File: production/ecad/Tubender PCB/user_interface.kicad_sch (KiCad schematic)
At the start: 10 parts, among them IC1 SN74HC138PWR, IC2 RA8875L3N, J7 4-1734592-0, U5 74HC595, U6 PEC11R-4215K-S0024

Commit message: Temp page added
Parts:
- added IC3: SN74LVC1G29DCTR, SOP65P400X130-8N, symbol SamacSys_Parts:SN74LVC1G29DCTR
- added IC4: SN74HC138PWR, SOP65P640X120-16N, symbol SamacSys_Parts:SN74HC138PWR
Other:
- moved on the sheet: DS1, IC1, U5

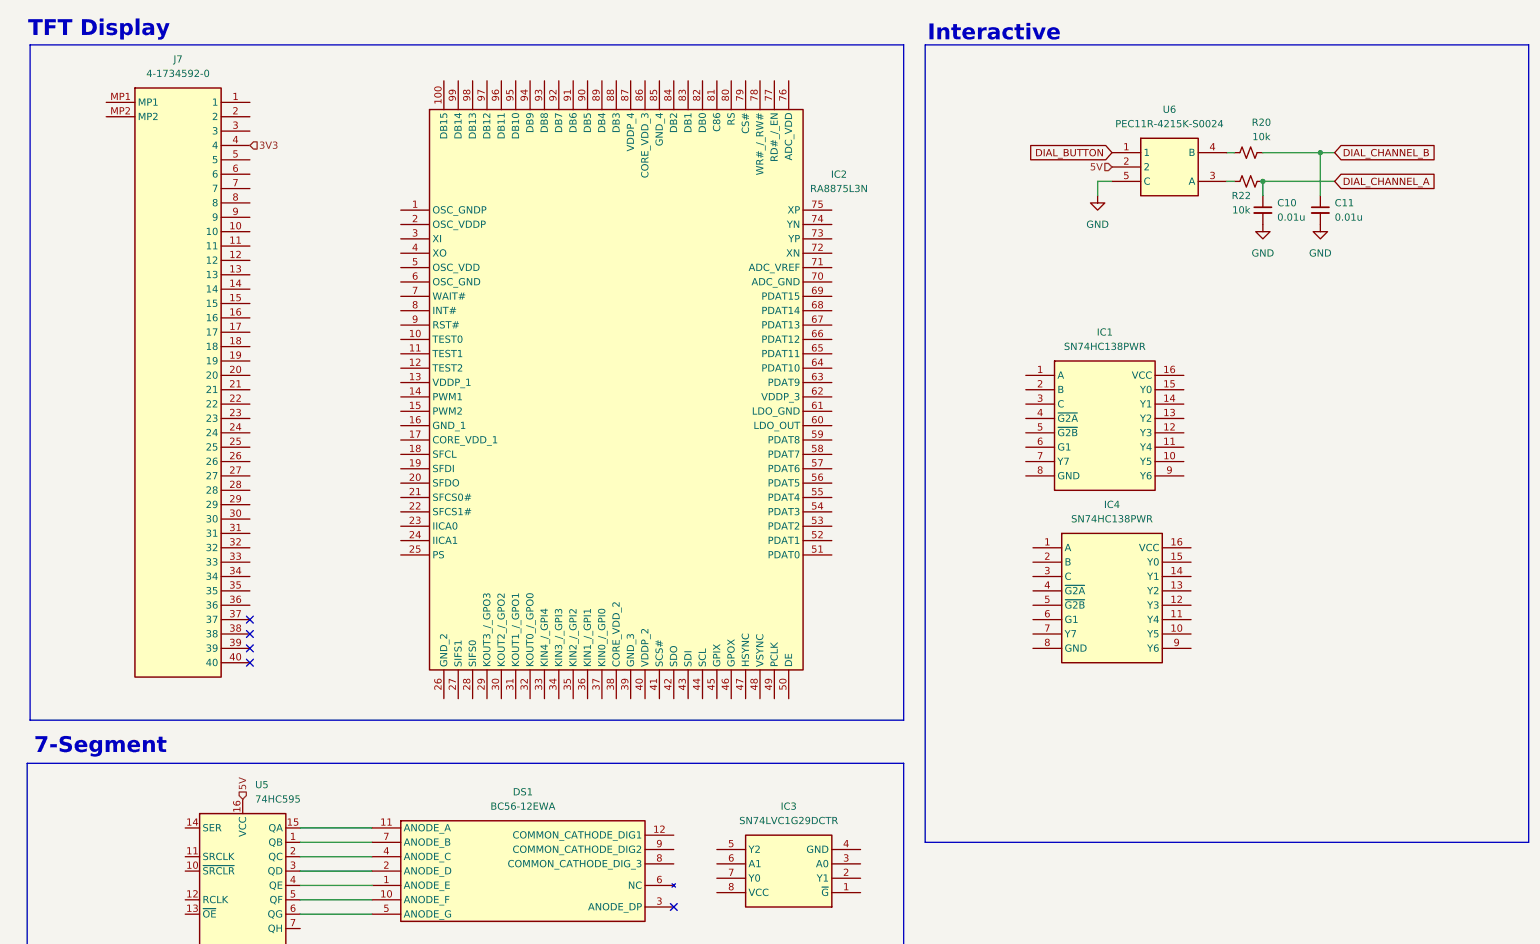
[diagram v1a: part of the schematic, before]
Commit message: Driver pin out
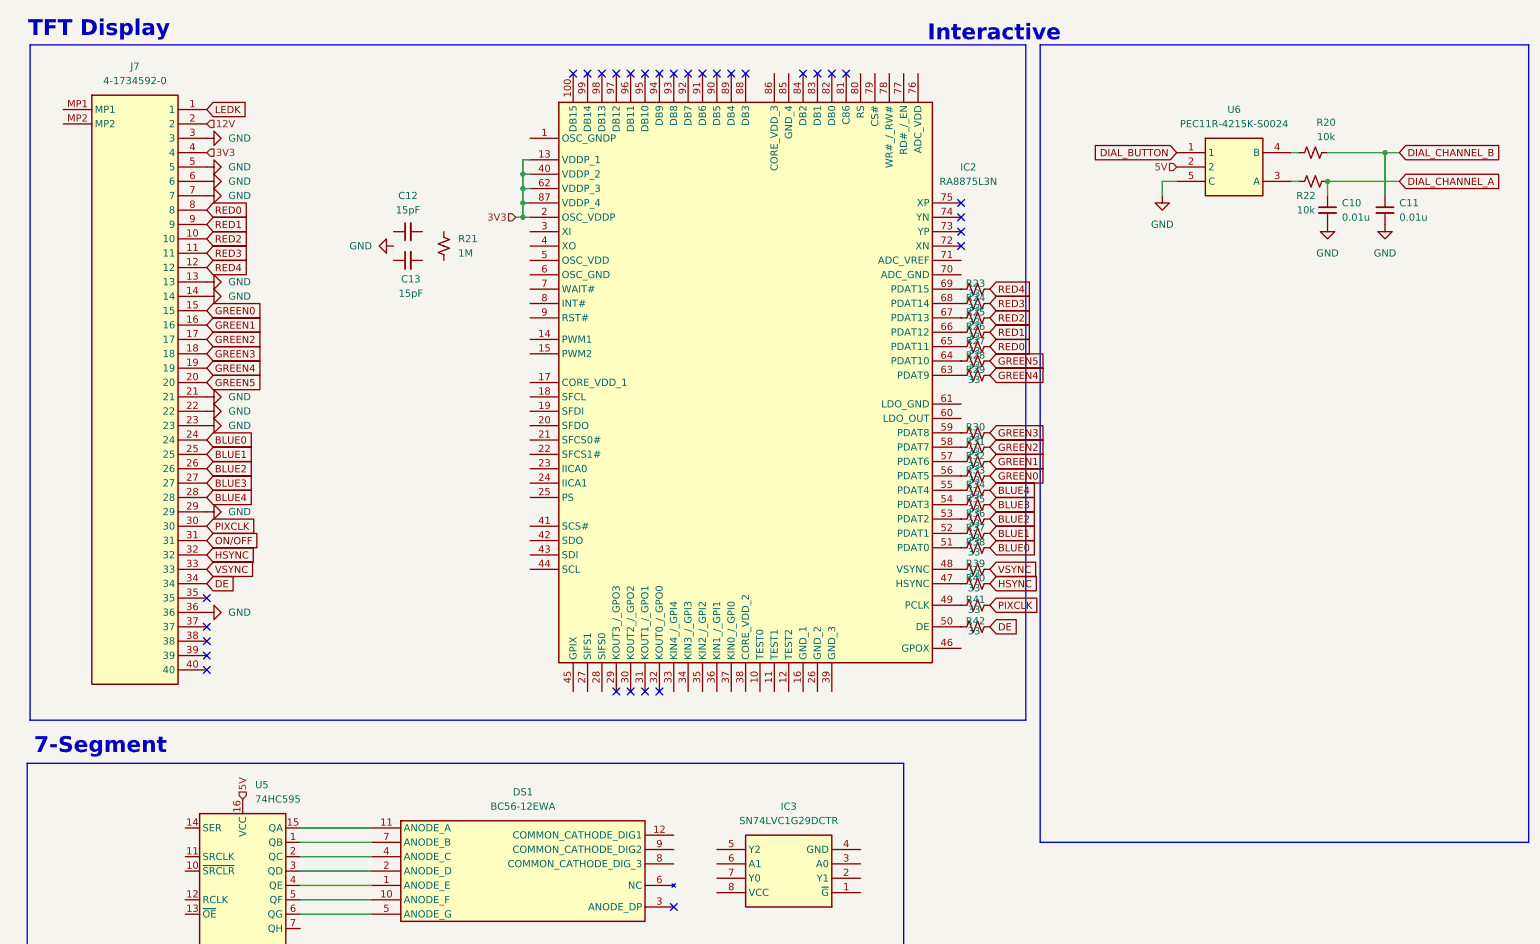
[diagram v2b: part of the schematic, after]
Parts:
- removed IC1, IC4: SN74HC138PWR, SOP65P640X120-16N, symbol SamacSys_Parts:SN74HC138PWR
- added C12, C13: 15pF, symbol Device:C_Small
- added R21: 1M, symbol Device:R_Small_US
- added R23, R24, R25, R26, R27, R28, R29, R30, R31, R32, R33, R34, R35, R36, R37, R38, R39, R40, R41, R42: 33, symbol Device:R_Small_US
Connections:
- net 3V3: now also IC2.13 (VDDP_1), IC2.2 (OSC_VDDP), IC2.40 (VDDP_2), IC2.62 (VDDP_3), IC2.87 (VDDP_4)
- net GND: now also J7.13, J7.14, J7.21, J7.22, J7.23, J7.29, J7.3, J7.36, J7.5, J7.6, J7.7
- net at IC2.47 (HSYNC): now also R40.1
- net at IC2.48 (VSYNC): now also R39.1
- net at IC2.49 (PCLK): now also R41.1
- net at IC2.50 (DE): now also R42.1
- net at IC2.51 (PDAT0): now also R38.1
- net at IC2.52 (PDAT1): now also R37.1
- net at IC2.53 (PDAT2): now also R36.1
- net at IC2.54 (PDAT3): now also R35.1
- net at IC2.55 (PDAT4): now also R34.1
- net at IC2.56 (PDAT5): now also R33.1
- net at IC2.57 (PDAT6): now also R32.1
- net at IC2.58 (PDAT7): now also R31.1
- net at IC2.59 (PDAT8): now also R30.1
- net at IC2.63 (PDAT9): now also R29.1
- net at IC2.64 (PDAT10): now also R28.1
- net at IC2.65 (PDAT11): now also R27.1
- net at IC2.66 (PDAT12): now also R26.1
- net at IC2.67 (PDAT13): now also R25.1
- net at IC2.68 (PDAT14): now also R24.1
- net at IC2.69 (PDAT15): now also R23.1
- net LEDK: now reaches J7.1
- net RED2: now reaches J7.10
- net RED2: now also R25.2
- net RED3: now reaches J7.11
- net RED3: now also R24.2
- net RED4: now reaches J7.12
- net RED4: now also R23.2
- net GREEN0: now reaches J7.15
- net GREEN0: now also R33.2
- net GREEN1: now reaches J7.16
- net GREEN1: now also R32.2
- net GREEN2: now reaches J7.17
- net GREEN2: now also R31.2
- net GREEN3: now reaches J7.18
- net GREEN3: now also R30.2
- net GREEN4: now reaches J7.19
- net GREEN4: now also R29.2
- net 12V: now reaches J7.2
- net GREEN5: now reaches J7.20
- net GREEN5: now also R28.2
- net BLUE0: now reaches J7.24
- net BLUE0: now also R38.2
- net BLUE1: now reaches J7.25
- net BLUE1: now also R37.2
- net BLUE2: now reaches J7.26
- net BLUE2: now also R36.2
- net BLUE3: now reaches J7.27
- net BLUE3: now also R35.2
- net BLUE4: now reaches J7.28
- net BLUE4: now also R34.2
- net PIXCLK: now reaches J7.30
- net PIXCLK: now also R41.2
- net ON/OFF: now reaches J7.31
- net HSYNC: now reaches J7.32
- net HSYNC: now also R40.2
- net VSYNC: now reaches J7.33
- net VSYNC: now also R39.2
- net DE: now reaches J7.34
- net DE: now also R42.2
- net RED0: now reaches J7.8
- net RED0: now also R27.2
- net RED1: now reaches J7.9
- net RED1: now also R26.2
- no-connect marks 5 -> 31
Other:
- moved on the sheet: C10, C11, IC2, J7, R20, R22, U6

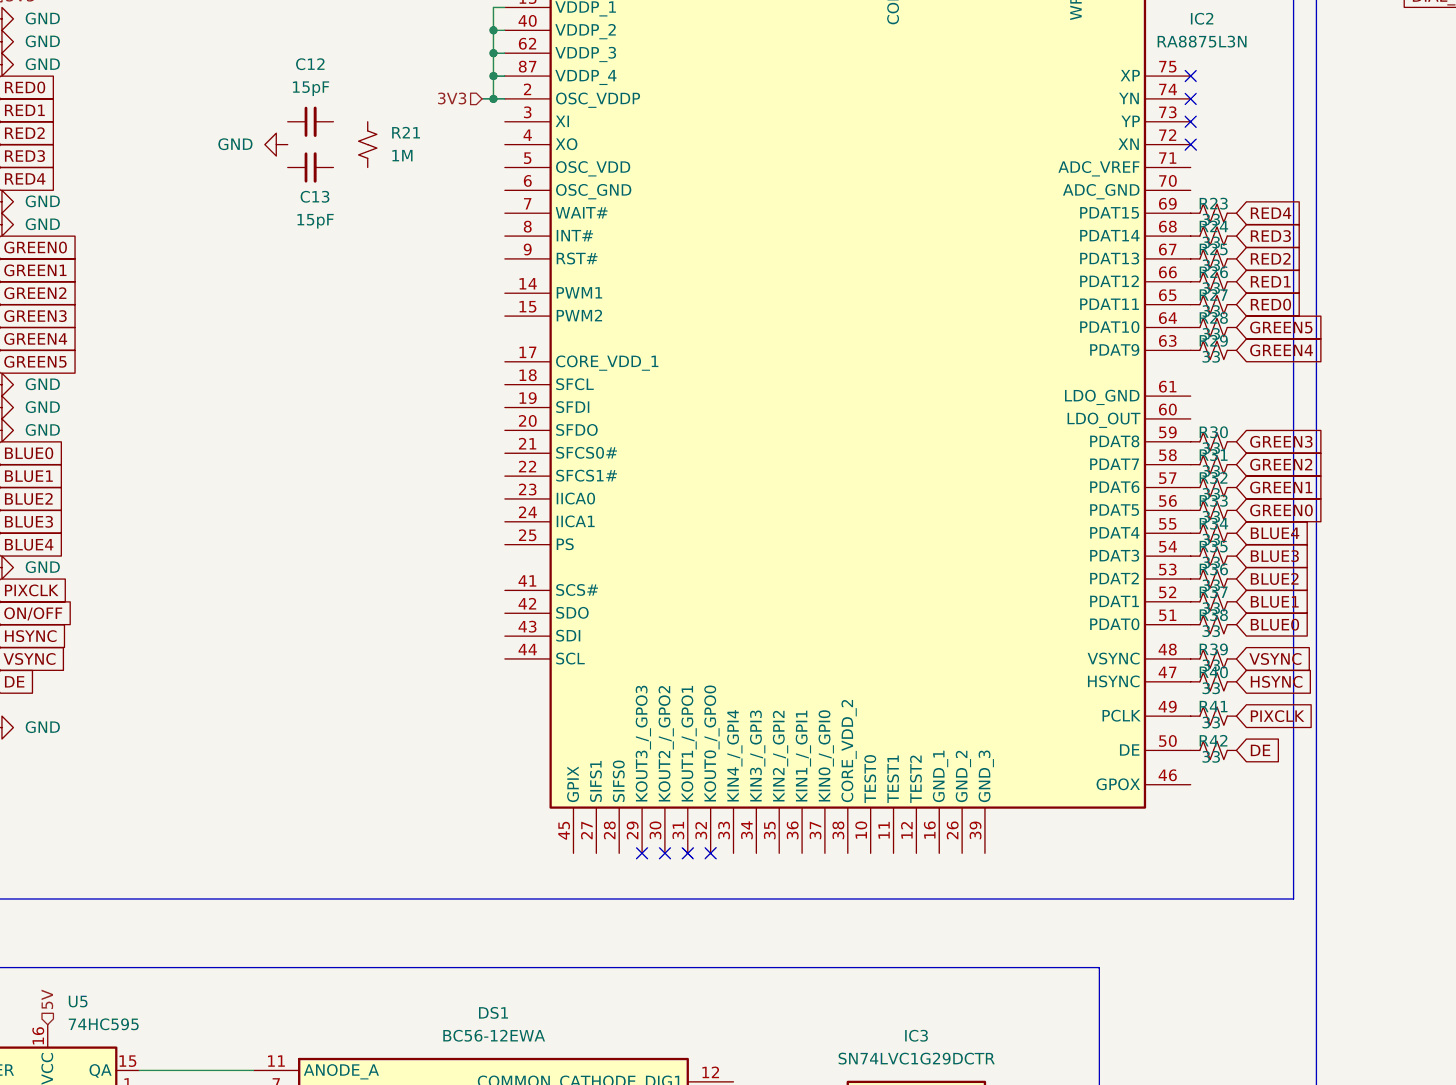
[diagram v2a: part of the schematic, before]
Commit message: More driver pins yay
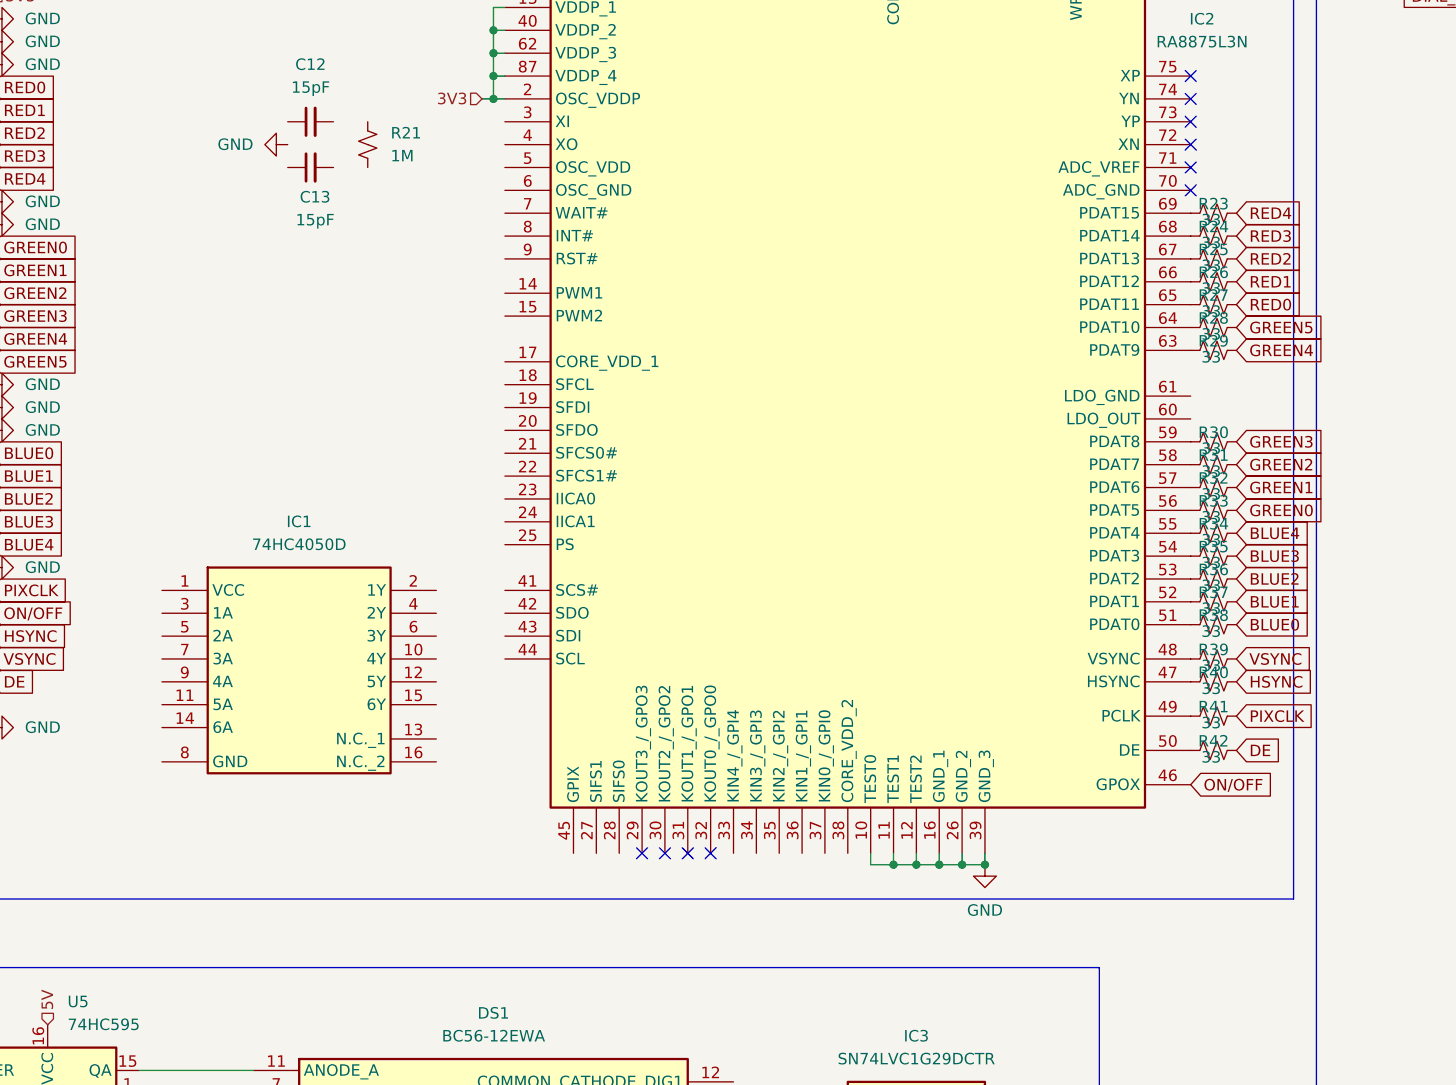
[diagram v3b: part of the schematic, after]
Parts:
- added IC1: 74HC4050D, SOIC127P600X175-16N, symbol SamacSys_Parts:74HC4050D
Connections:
- net GND: now also IC2.10 (TEST0), IC2.11 (TEST1), IC2.12 (TEST2), IC2.16 (GND_1), IC2.26 (GND_2), IC2.39 (GND_3)
- net ON/OFF: now also IC2.46 (GPOX)
- no-connect marks 31 -> 33
